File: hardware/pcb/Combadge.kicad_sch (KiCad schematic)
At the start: 21 parts, among them J1 Conn_01x02_Female, J2 Conn_01x02_Female, J3 TOUCH, U1 ESP32-WROOM-32, U2 MAX98357AEWL+T

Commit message: Make all resistors 1206 and LEDs 0805
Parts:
- D2: footprint LED_SMD:LED_1206_3216Metric_Pad1.42x1.75mm_HandSolder -> LED_SMD:LED_0805_2012Metric_Pad1.15x1.40mm_HandSolder
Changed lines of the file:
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@@
       (effects (font (size 1.27 1.27)))
     )
-    (property "Footprint" "LED_SMD:LED_1206_3216Metric_Pad1.42x1.75mm_HandSolder" (at 114.3 93.98 0)
+    (property "Footprint" "LED_SMD:LED_0805_2012Metric_Pad1.15x1.40mm_HandSolder" (at 114.3 93.98 0)
       (effects (font (size 1.27 1.27)) hide)
     )

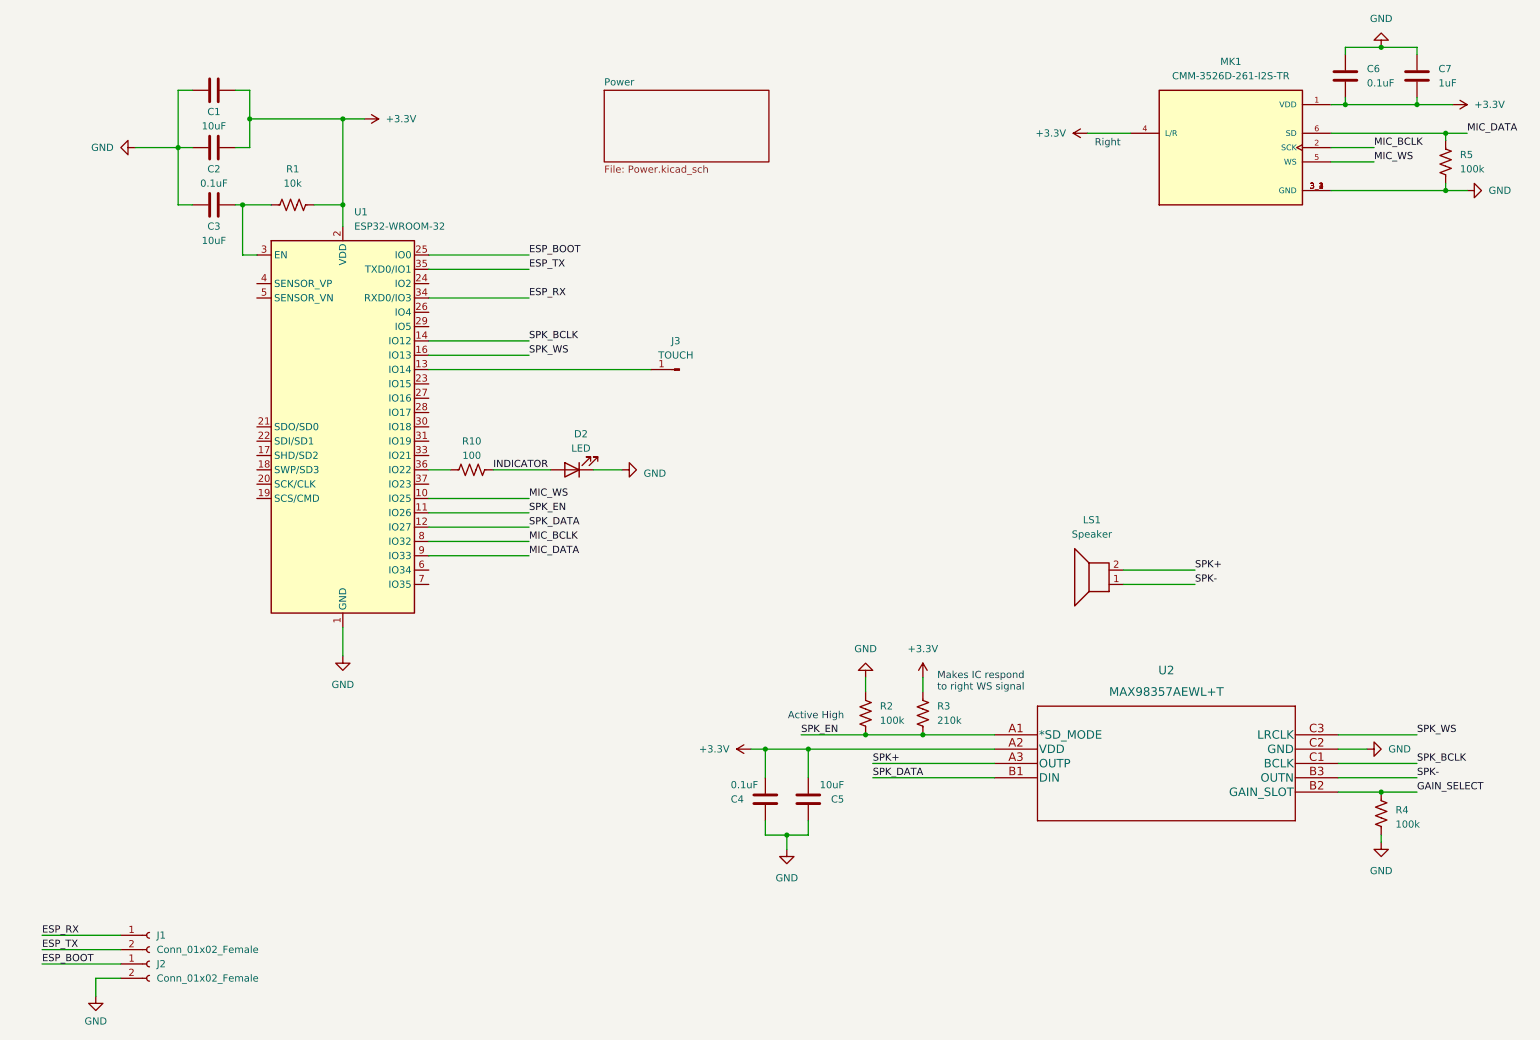
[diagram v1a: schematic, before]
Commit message: Switch to TLV4333PDBVR LDO regulator
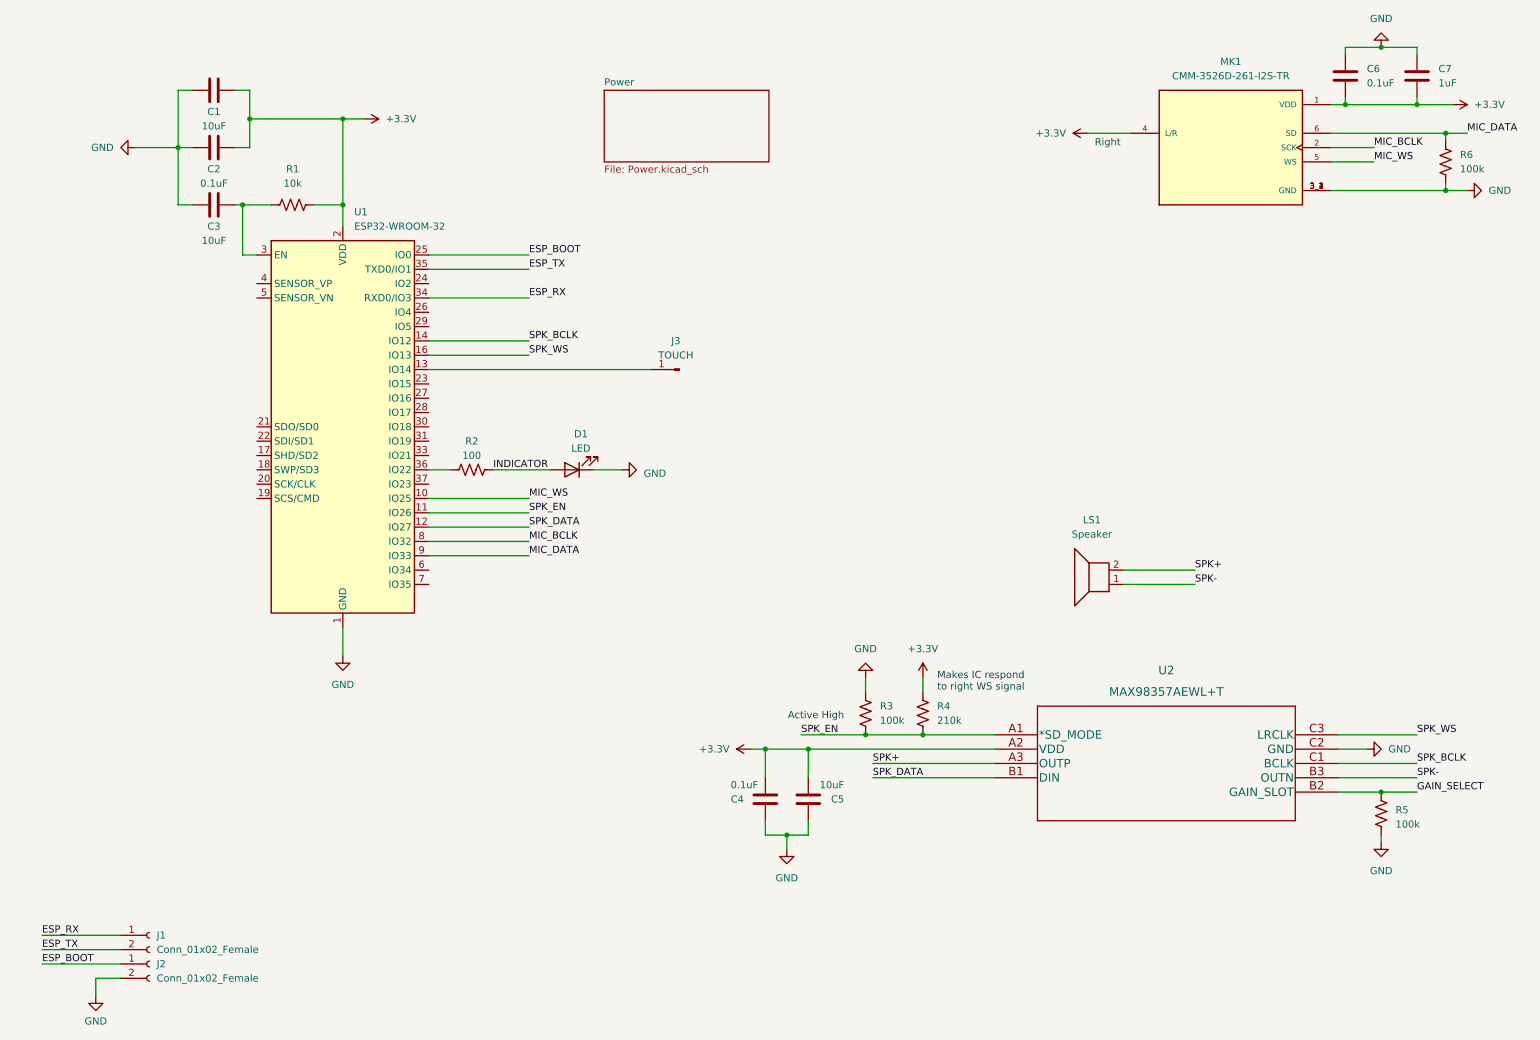
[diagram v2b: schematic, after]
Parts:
- renumbered D2 to D1, R10 to R2, R2 to R3, R3 to R4, R4 to R5, R5 to R6

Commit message: Replace BGA IC with QFN
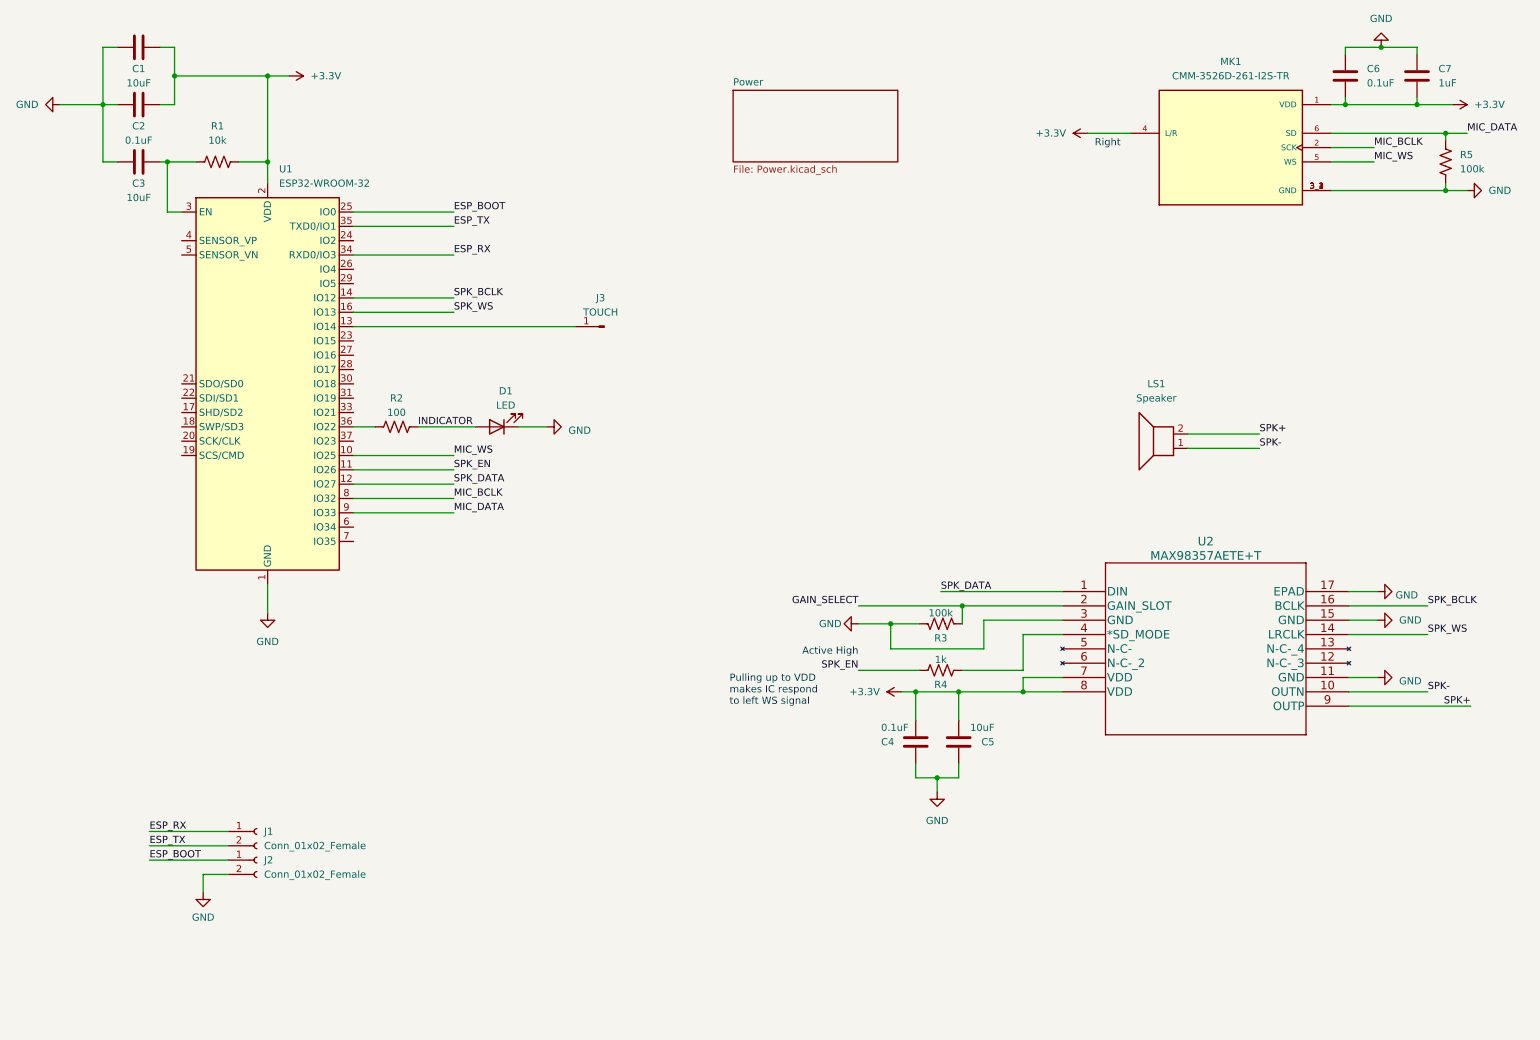
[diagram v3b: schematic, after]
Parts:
- removed R3: 100k, Resistor_SMD:R_1206_3216Metric_Pad1.30x1.75mm_HandSolder, symbol Device:R_US
- removed U2: MAX98357AEWL+T, MAX98357AEWL+T:MAX98357AEWL&plus_T, symbol MAX98357AEWL+T:MAX98357AEWL+T
- added U2: MAX98357AETE+T, MAX98357AETE+T:MAX98357AETE&plus_T, symbol MAX98357AETE+T:MAX98357AETE+T
- R4: value 210k -> 1k
- renumbered R5 to R3, R6 to R5
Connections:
- net +3.3V: now also U2.7 (VDD), U2.8 (VDD); no longer R4.1
- net GAIN_SELECT: now also R3.2, U2.2 (GAIN_SLOT); no longer R3.1
- net GND: now also R3.1, U2.11 (GND), U2.15 (GND), U2.17 (EPAD), U2.3 (GND); no longer R3.2
- net SPK+: now also U2.9 (OUTP)
- net SPK-: now also U2.10 (OUTN)
- net SPK_BCLK: now also U2.16 (BCLK)
- net SPK_DATA: now also U2.1 (DIN)
- net SPK_EN: now also R4.1; no longer R4.2
- net SPK_WS: now also U2.14 (LRCLK)
- new net: R4.2, U2.4 (*SD_MODE)
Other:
- note added: "Pulling up to VDD makes IC respond to left WS signal"
- note removed: "Makes IC respond to right WS signal"
- moved on the sheet: C1, C2, C3, C4, C5, D1, J1, J2, J3, LS1, R1, R2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

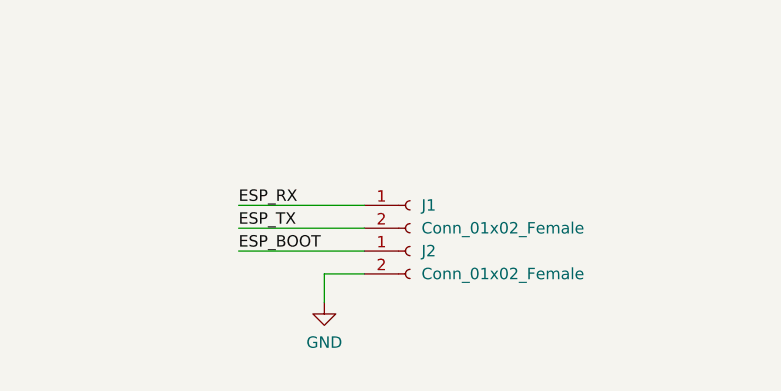
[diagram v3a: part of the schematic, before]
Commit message: Add ESP32 boot button
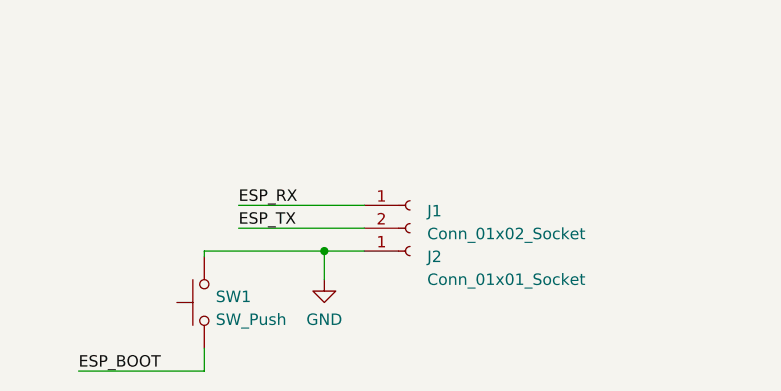
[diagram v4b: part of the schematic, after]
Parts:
- removed J1, J2: Conn_01x02_Female, Connector_PinHeader_2.54mm:PinHeader_1x02_P2.54mm_Vertical, symbol Connector:Conn_01x02_Female
- added J1: Conn_01x02_Socket, Connector_PinHeader_2.54mm:PinHeader_1x02_P2.54mm_Vertical, symbol Connector:Conn_01x02_Socket
- added J2: Conn_01x01_Socket, Connector_PinHeader_2.54mm:PinHeader_1x01_P2.54mm_Vertical, symbol Connector:Conn_01x01_Socket
- added SW1: SW_Push, Button_Switch_SMD:SW_SPST_CK_RS282G05A3, symbol Switch:SW_Push
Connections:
- net ESP_BOOT: now also SW1.1
- net ESP_RX: now also J1.1 (Pin_1)
- net ESP_TX: now also J1.2 (Pin_2)
- net GND: now also J2.1 (Pin_1), SW1.2
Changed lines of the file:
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@@
   (junction (at 42.545 39.37) (diameter 0) (color 0 0 0 0)
   )
+  (junction (at 48.895 163.195) (diameter 0) (color 0 0 0 0)
+  )
   (junction (at 183.515 118.11) (diameter 0) (color 0 0 0 0)
   )
@@
     (stroke (width 0) (type default))
   )
+  (wire (pts (xy 35.56 163.83) (xy 35.56 163.195))
+    (stroke (width 0) (type default))
+  )
   (wire (pts (xy 252.095 120.65) (xy 257.175 120.65))
     (stroke (width 0) (type default))
@@
     (stroke (width 0) (type default))
   )
+  (wire (pts (xy 48.895 163.195) (xy 53.34 163.195))
+    (stroke (width 0) (type default))
+  )
   (wire (pts (xy 252.095 130.81) (xy 257.175 130.81))
     (stroke (width 0) (type default))
@@
     (stroke (width 0) (type default))
   )
-  (wire (pts (xy 53.34 165.735) (xy 48.895 165.735))
+  (wire (pts (xy 35.56 163.195) (xy 48.895 163.195))
     (stroke (width 0) (type default))
   )
@@
     (stroke (width 0) (type default))
   )
-  (wire (pts (xy 48.895 165.735) (xy 48.895 168.91))
-    (stroke (width 0) (type default))
-  )
-  (wire (pts (xy 39.37 163.195) (xy 53.34 163.195))
+  (wire (pts (xy 48.895 163.195) (xy 48.895 166.37))
+    (stroke (width 0) (type default))
+  )
+  (wire (pts (xy 21.59 176.53) (xy 35.56 176.53))
     (stroke (width 0) (type default))
   )
@@
   )
   (wire (pts (xy 257.81 19.05) (xy 264.16 19.05))
+    (stroke (width 0) (type default))
+  )
+  (wire (pts (xy 35.56 176.53) (xy 35.56 173.99))
     (stroke (width 0) (type default))
   )
@@
     (effects (font (size 1.27 1.27)) (justify left bottom))
   )
-  (label "ESP_BOOT" (at 39.37 163.195 0) (fields_autoplaced)
+  (label "ESP_BOOT" (at 21.59 176.53 0) (fields_autoplaced)
     (effects (font (size 1.27 1.27)) (justify left bottom))
   )
@@
     (effects (font (size 1.27 1.27)) (justify left bottom))
   )
+  (symbol (lib_id "Connector:Conn_01x02_Socket") (at 58.42 158.115 0) (unit 1)
+    (in_bom yes) (on_board yes) (dnp no) (fields_autoplaced)
+    (property "Reference" "J1" (at 60.325 158.75 0)
+      (effects (font (size 1.27 1.27)) (justify left))
+    )
+    (property "Value" "Conn_01x02_Socket" (at 60.325 161.29 0)
+      (effects (font (size 1.27 1.27)) (justify left))
+    )
+    (property "Footprint" "Connector_PinHeader_2.54mm:PinHeader_1x02_P2.54mm_Vertical" (at 58.42 158.115 0)
+      (effects (font (size 1.27 1.27)) hide)
+    )
+    (property "Datasheet" "~" (at 58.42 158.115 0)
+      (effects (font (size 1.27 1.27)) hide)
+    )
+    (pin "1")
+    (pin "2")
+    (instances
+      (project "Combadge"
+        (path "/dc42e7bc-f663-434d-8744-232038ac4fdf"
+          (reference "J1") (unit 1)
+        )
+      )
+    )
+  )
   (symbol (lib_id "power:+3.3V") (at 172.72 133.35 90) (unit 1)
     (in_bom yes) (on_board yes) (dnp no) (fields_autoplaced)
@@
     )
   )
-  (symbol (lib_id "power:GND") (at 48.895 168.91 0) (unit 1)
-    (in_bom yes) (on_board yes) (dnp no) (fields_autoplaced)
-    (property "Reference" "#PWR02" (at 48.895 175.26 0)
-      (effects (font (size 1.27 1.27)) hide)
-    )
-    (property "Value" "GND" (at 48.895 173.355 0)
-      (effects (font (size 1.27 1.27)))
-    )
-    (property "Footprint" "" (at 48.895 168.91 0)
-      (effects (font (size 1.27 1.27)) hide)
-    )
-    (property "Datasheet" "" (at 48.895 168.91 0)
+  (symbol (lib_id "power:GND") (at 48.895 166.37 0) (unit 1)
+    (in_bom yes) (on_board yes) (dnp no) (fields_autoplaced)
+    (property "Reference" "#PWR02" (at 48.895 172.72 0)
+      (effects (font (size 1.27 1.27)) hide)
+    )
+    (property "Value" "GND" (at 48.895 170.815 0)
+      (effects (font (size 1.27 1.27)))
+    )
+    (property "Footprint" "" (at 48.895 166.37 0)
+      (effects (font (size 1.27 1.27)) hide)
+    )
+    (property "Datasheet" "" (at 48.895 166.37 0)
       (effects (font (size 1.27 1.27)) hide)
     )
@@
     )
   )
-  (symbol (lib_id "Connector:Conn_01x02_Female") (at 58.42 158.115 0) (unit 1)
-    (in_bom yes) (on_board yes) (dnp no) (fields_autoplaced)
-    (property "Reference" "J1" (at 59.69 158.1149 0)
+  (symbol (lib_id "Connector:Conn_01x01_Socket") (at 58.42 163.195 0) (unit 1)
+    (in_bom yes) (on_board yes) (dnp no)
+    (property "Reference" "J2" (at 60.325 163.83 0)
       (effects (font (size 1.27 1.27)) (justify left))
     )
-    (property "Value" "Conn_01x02_Female" (at 59.69 160.6549 0)
+    (property "Value" "Conn_01x01_Socket" (at 60.325 166.37 0)
       (effects (font (size 1.27 1.27)) (justify left))
     )
-    (property "Footprint" "Connector_PinHeader_2.54mm:PinHeader_1x02_P2.54mm_Vertical" (at 58.42 158.115 0)
-      (effects (font (size 1.27 1.27)) hide)
-    )
-    (property "Datasheet" "~" (at 58.42 158.115 0)
+    (property "Footprint" "Connector_PinHeader_2.54mm:PinHeader_1x01_P2.54mm_Vertical" (at 58.42 163.195 0)
+      (effects (font (size 1.27 1.27)) hide)
+    )
+    (property "Datasheet" "~" (at 58.42 163.195 0)
+      (effects (font (size 1.27 1.27)) hide)
+    )
+    (pin "1")
+    (instances
+      (project "Combadge"
+        (path "/dc42e7bc-f663-434d-8744-232038ac4fdf"
+          (reference "J2") (unit 1)
+        )
+      )
+    )
+  )
+  (symbol (lib_id "Switch:SW_Push") (at 35.56 168.91 90) (unit 1)
+    (in_bom yes) (on_board yes) (dnp no) (fields_autoplaced)
+    (property "Reference" "SW1" (at 36.83 168.275 90)
+      (effects (font (size 1.27 1.27)) (justify right))
+    )
+    (property "Value" "SW_Push" (at 36.83 170.815 90)
+      (effects (font (size 1.27 1.27)) (justify right))
+    )
+    (property "Footprint" "Button_Switch_SMD:SW_SPST_CK_RS282G05A3" (at 30.48 168.91 0)
+      (effects (font (size 1.27 1.27)) hide)
+    )
+    (property "Datasheet" "~" (at 30.48 168.91 0)
       (effects (font (size 1.27 1.27)) hide)
     )
@@
       (project "Combadge"
         (path "/dc42e7bc-f663-434d-8744-232038ac4fdf"
-          (reference "J1") (unit 1)
-        )
-      )
-    )
-  )
-  (symbol (lib_id "Connector:Conn_01x02_Female") (at 58.42 163.195 0) (unit 1)
-    (in_bom yes) (on_board yes) (dnp no) (fields_autoplaced)
-    (property "Reference" "J2" (at 59.69 163.1949 0)
-      (effects (font (size 1.27 1.27)) (justify left))
-    )
-    (property "Value" "Conn_01x02_Female" (at 59.69 165.7349 0)
-      (effects (font (size 1.27 1.27)) (justify left))
-    )
-    (property "Footprint" "Connector_PinHeader_2.54mm:PinHeader_1x02_P2.54mm_Vertical" (at 58.42 163.195 0)
-      (effects (font (size 1.27 1.27)) hide)
-    )
-    (property "Datasheet" "~" (at 58.42 163.195 0)
-      (effects (font (size 1.27 1.27)) hide)
-    )
-    (pin "1")
-    (pin "2")
-    (instances
-      (project "Combadge"
-        (path "/dc42e7bc-f663-434d-8744-232038ac4fdf"
-          (reference "J2") (unit 1)
-        )
-      )
+          (reference "SW1") (unit 1)
+        )
+      )
